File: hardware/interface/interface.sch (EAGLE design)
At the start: 12 parts

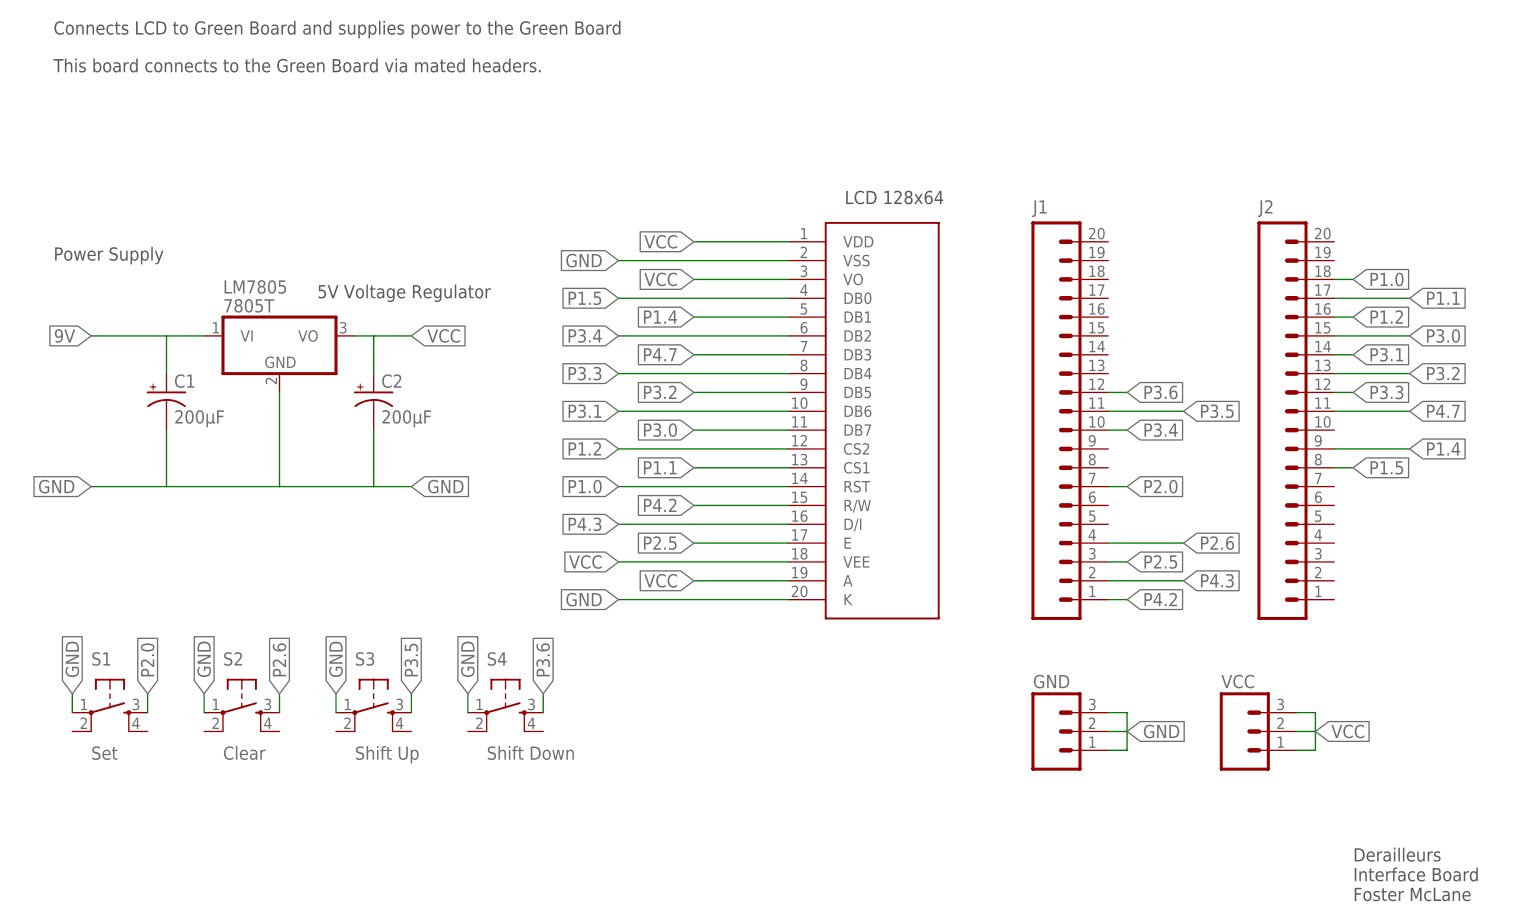
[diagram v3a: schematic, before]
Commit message: Finish routing all boards, schematics are consitant, and all deliverable requirements are met..
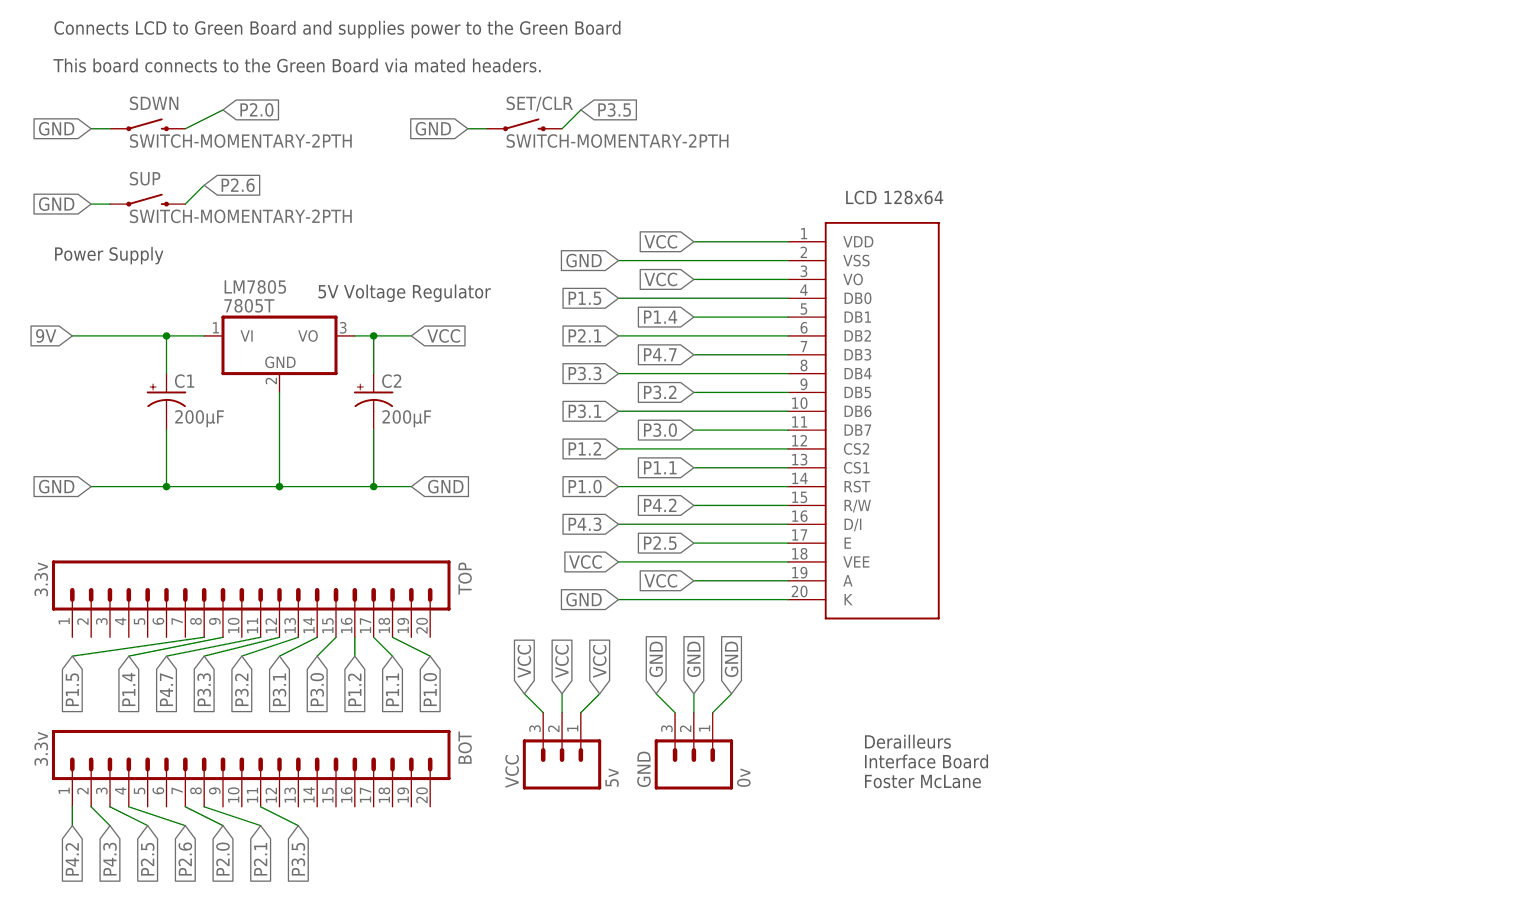
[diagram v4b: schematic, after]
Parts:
- removed J1, J2: (no value), SparkFun-Connectors:M20
- removed S1: Set, SparkFun-Retired:TAC_SWITCHPTH
- removed S2: Clear, SparkFun-Retired:TAC_SWITCHPTH
- removed S3: Shift Up, SparkFun-Retired:TAC_SWITCHPTH
- removed S4: Shift Down, SparkFun-Retired:TAC_SWITCHPTH
- added BOT, TOP: 3.3v, SparkFun-Connectors:M20
- added SDWN, SET/CLR, SUP: SWITCH-MOMENTARY-2PTH, SparkFun-Electromechanical:SWITCH-MOMENTARY-2PTH
- GND: value (none) -> 0v
- VCC: value (none) -> 5v
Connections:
- removed net P3.4: J1.10, U$1.DB2
- removed net P3.6: J1.12, S4.3
- new net P2.1: BOT.8, U$1.DB2
- net GND: now also SDWN.1, SET/CLR.1, SUP.1; no longer S1.1, S2.1, S3.1, S4.1
- net P1.0: now also TOP.18; no longer J2.18
- net P1.1: now also TOP.17; no longer J2.17
- net P1.2: now also TOP.16; no longer J2.16
- net P1.4: now also TOP.9; no longer J2.9
- net P1.5: now also TOP.8; no longer J2.8
- net P2.0: now also BOT.7, SDWN.2; no longer J1.7, S1.3
- net P2.5: now also BOT.3; no longer J1.3
- net P2.6: now also BOT.4, SUP.2; no longer J1.4, S2.3
- net P3.0: now also TOP.15; no longer J2.15
- net P3.1: now also TOP.14; no longer J2.14
- net P3.2: now also TOP.13; no longer J2.13
- net P3.3: now also TOP.12; no longer J2.12
- net P3.5: now also BOT.11, SET/CLR.2; no longer J1.11, S3.3
- net P4.2: now also BOT.1; no longer J1.1
- net P4.3: now also BOT.2; no longer J1.2
- net P4.7: now also TOP.11; no longer J2.11
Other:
- moved on the sheet: GND, VCC
